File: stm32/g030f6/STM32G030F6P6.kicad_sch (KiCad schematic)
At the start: 18 parts, among them J1 STLINK, J2 LEFT, J3 RIGHT, U1 XC6220B331MR, U2 STM32G030F6Px

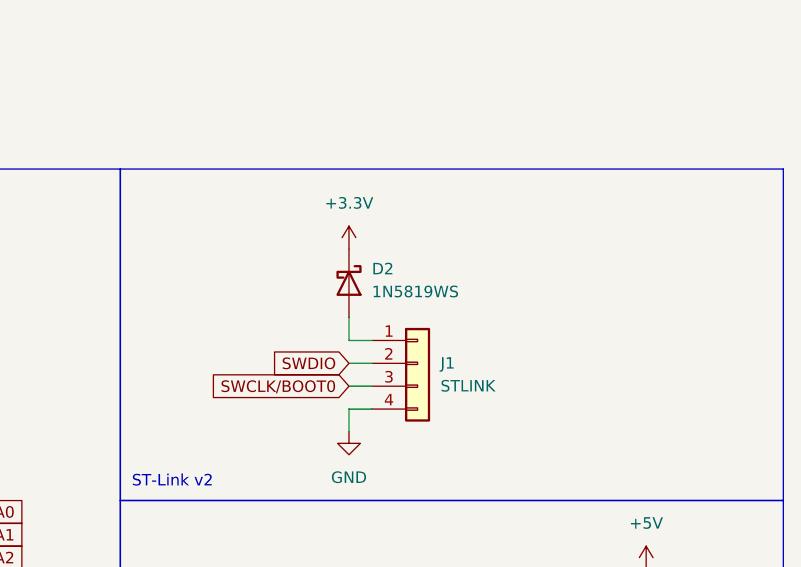
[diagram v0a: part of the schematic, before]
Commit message: WIP: F070F6P6, Fix: Diode direction corrected for F042F6P6.
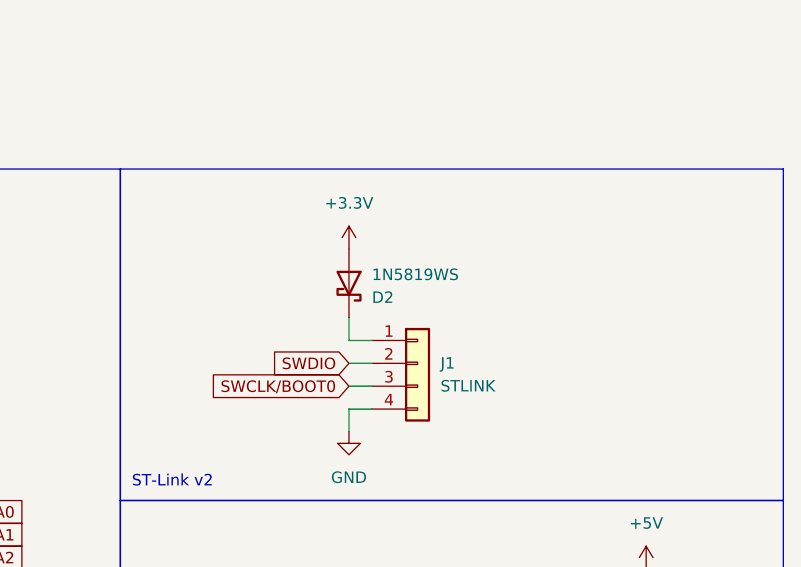
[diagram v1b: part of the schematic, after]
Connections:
- net +3.3V: now also D2.2 (A); no longer D2.1 (K)
- net at J1.1 (Pin_1): now also D2.1 (K); no longer D2.2 (A)
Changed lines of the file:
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@@
     )
   )
-  (symbol (lib_id "Diode:1N5819WS") (at 176.53 72.39 270) (unit 1)
+  (symbol (lib_id "Diode:1N5819WS") (at 176.53 72.39 270) (mirror x) (unit 1)
     (in_bom yes) (on_board yes) (dnp no)
-    (property "Reference" "D2" (at 179.07 70.8025 90)
+    (property "Reference" "D2" (at 179.07 73.9775 90)
       (effects (font (size 1.27 1.27)) (justify left))
     )
-    (property "Value" "1N5819WS" (at 179.07 73.3425 90)
+    (property "Value" "1N5819WS" (at 179.07 71.4375 90)
       (effects (font (size 1.27 1.27)) (justify left))
     )

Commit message: Fix: Diode direction corrected.
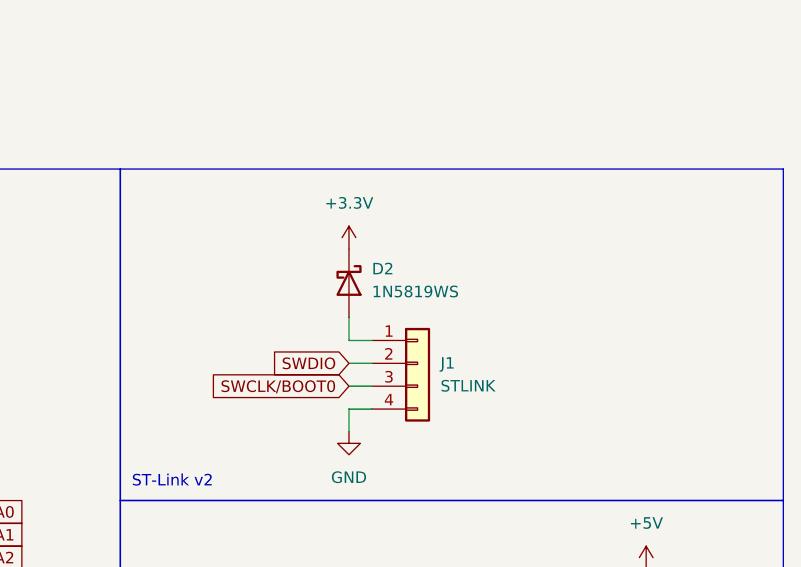
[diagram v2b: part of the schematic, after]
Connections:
- net +3.3V: now also D2.1 (K); no longer D2.2 (A)
- net at J1.1 (Pin_1): now also D2.2 (A); no longer D2.1 (K)
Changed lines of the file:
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@@
     )
   )
-  (symbol (lib_id "Diode:1N5819WS") (at 176.53 72.39 270) (mirror x) (unit 1)
+  (symbol (lib_id "Diode:1N5819WS") (at 176.53 72.39 270) (unit 1)
     (in_bom yes) (on_board yes) (dnp no)
-    (property "Reference" "D2" (at 179.07 73.9775 90)
+    (property "Reference" "D2" (at 179.07 70.8025 90)
       (effects (font (size 1.27 1.27)) (justify left))
     )
-    (property "Value" "1N5819WS" (at 179.07 71.4375 90)
+    (property "Value" "1N5819WS" (at 179.07 73.3425 90)
       (effects (font (size 1.27 1.27)) (justify left))
     )

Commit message: Update 2023-11-27
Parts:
- R4: value 10k -> 1k
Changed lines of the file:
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@@
       (effects (font (size 1.27 1.27)))
     )
-    (property "Value" "10k" (at 67.31 50.8 90)
+    (property "Value" "1k" (at 67.31 50.8 90)
       (effects (font (size 1.27 1.27)))
     )
